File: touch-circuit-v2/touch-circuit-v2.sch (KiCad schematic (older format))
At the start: 14 parts, among them Q1 Q_PMOS_GSD, Q2 Q_NMOS_GSD

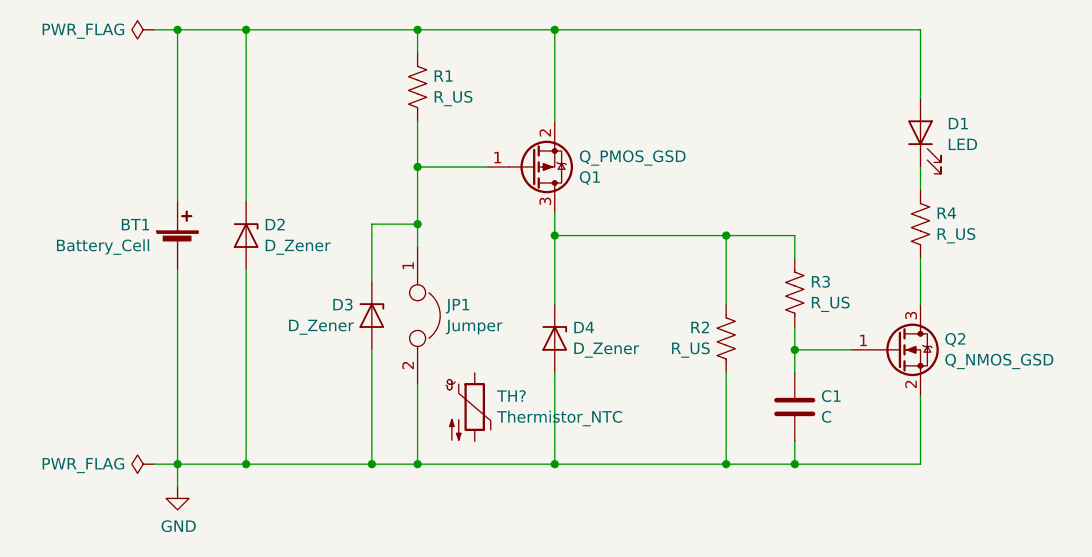
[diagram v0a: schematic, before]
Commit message: update schematic for high side jumper
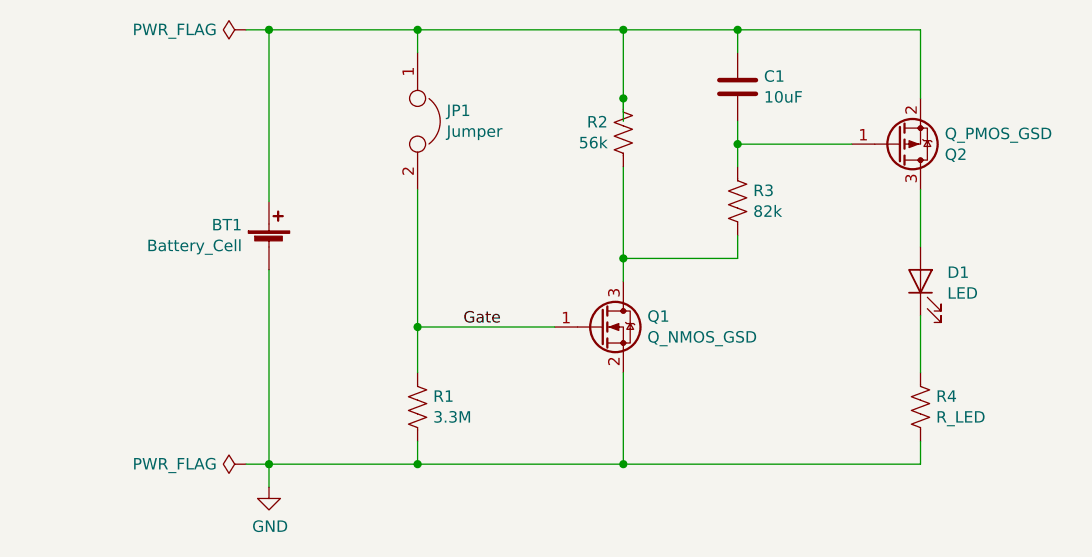
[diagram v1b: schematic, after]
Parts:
- removed D2, D3, D4: D_Zener, Diode_SMD:D_0805_2012Metric_Pad1.15x1.40mm_HandSolder, symbol Device:D_Zener
- removed TH?: Thermistor_NTC, symbol Device:Thermistor_NTC
- C1: value C -> 10uF
- R1: value R_US -> 3.3M
- R2: value R_US -> 56k
- R3: value R_US -> 82k
- R4: value R_US -> R_LED
- renumbered Q2 to Q1, Q1 to Q2
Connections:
- net labels added: Gate
- wire segments 44 -> 32
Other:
- moved on the sheet: BT1, C1, D1, JP1, Q1, Q2, R1, R2, R3, R4
